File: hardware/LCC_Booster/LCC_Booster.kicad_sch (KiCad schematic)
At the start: 16 parts, among them J1 A00-216-262-450, J2 54-00166, J3 Screw_Terminal_01x08, SW1 SW_Push, U1 ACPL-214-500E, U2 ACPL-214-500E

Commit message: Update Schematic
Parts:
- removed C34, C35: C100n, Capacitor_SMD:C_0402_1005Metric_Pad0.74x0.62mm_HandSolder, symbol Device:C
- removed U1, U2: ACPL-214-500E, Package_SO:SOP-4_4.4x2.6mm_P1.27mm, symbol Isolator:ACPL-214-500E
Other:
- added sheet DCC Isolator (dcc_isolator.kicad_sch)
- moved on the sheet: A1, H1, H2, H3, H4, J1A, J1B, J2, J3, JP1, JP2, JP3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

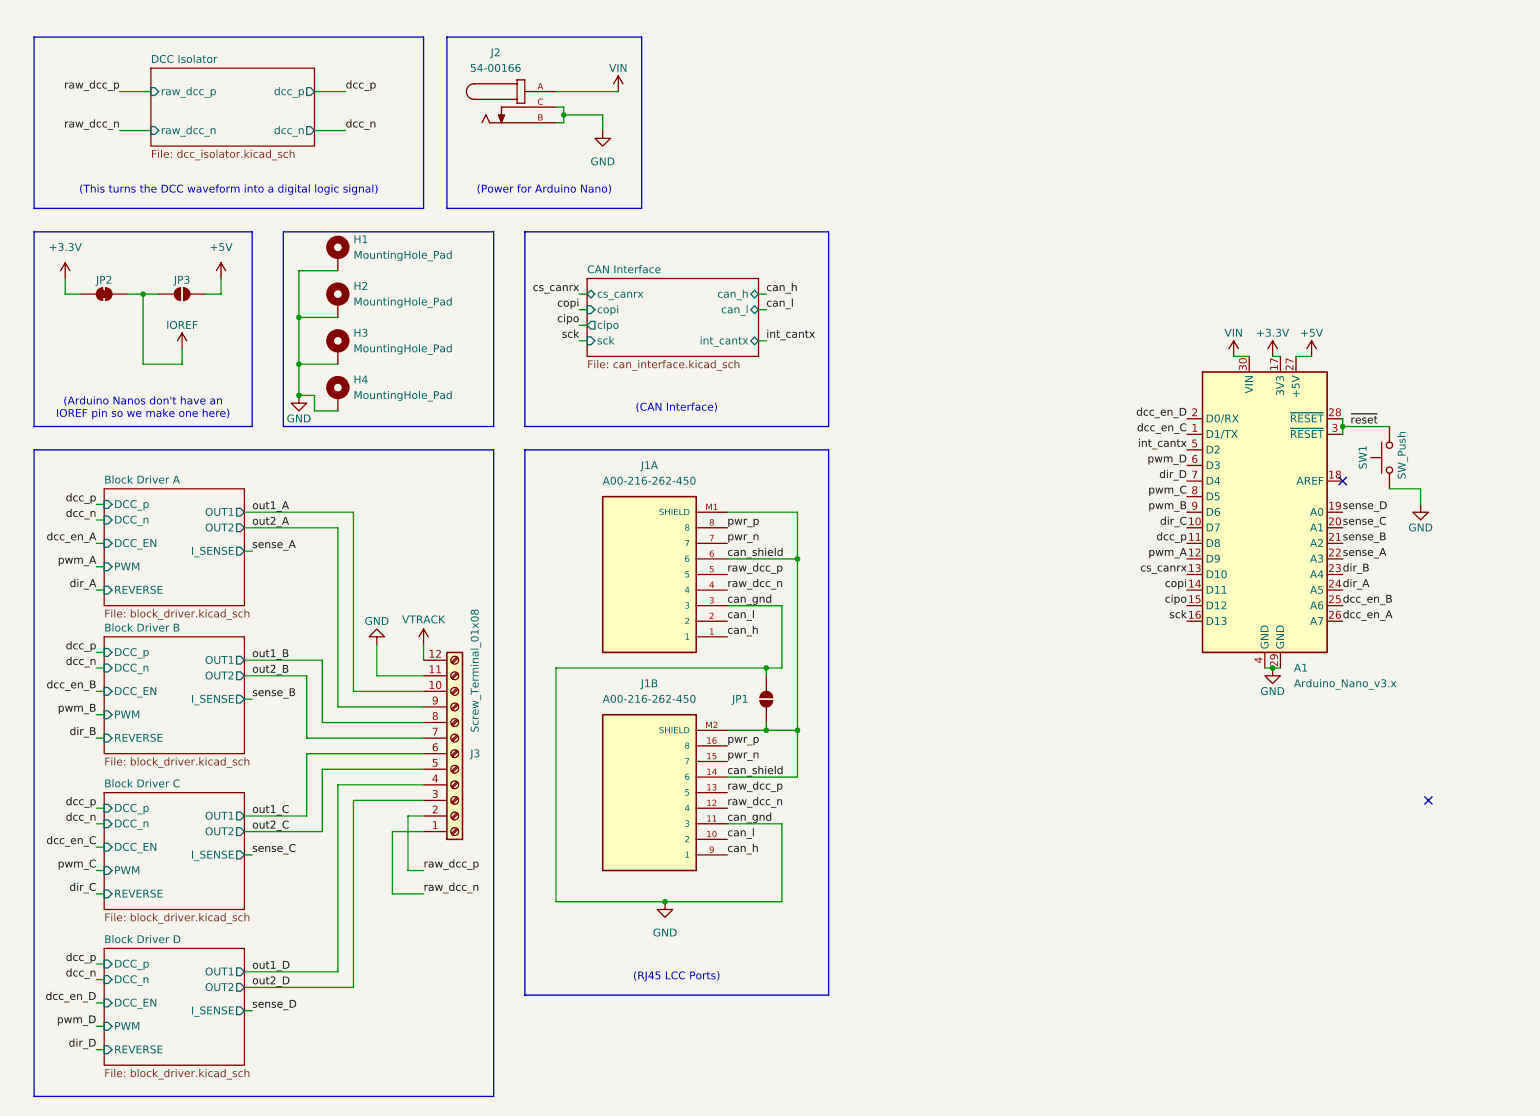
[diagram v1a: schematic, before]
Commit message: Add Fault Pin Inputs to Arduino
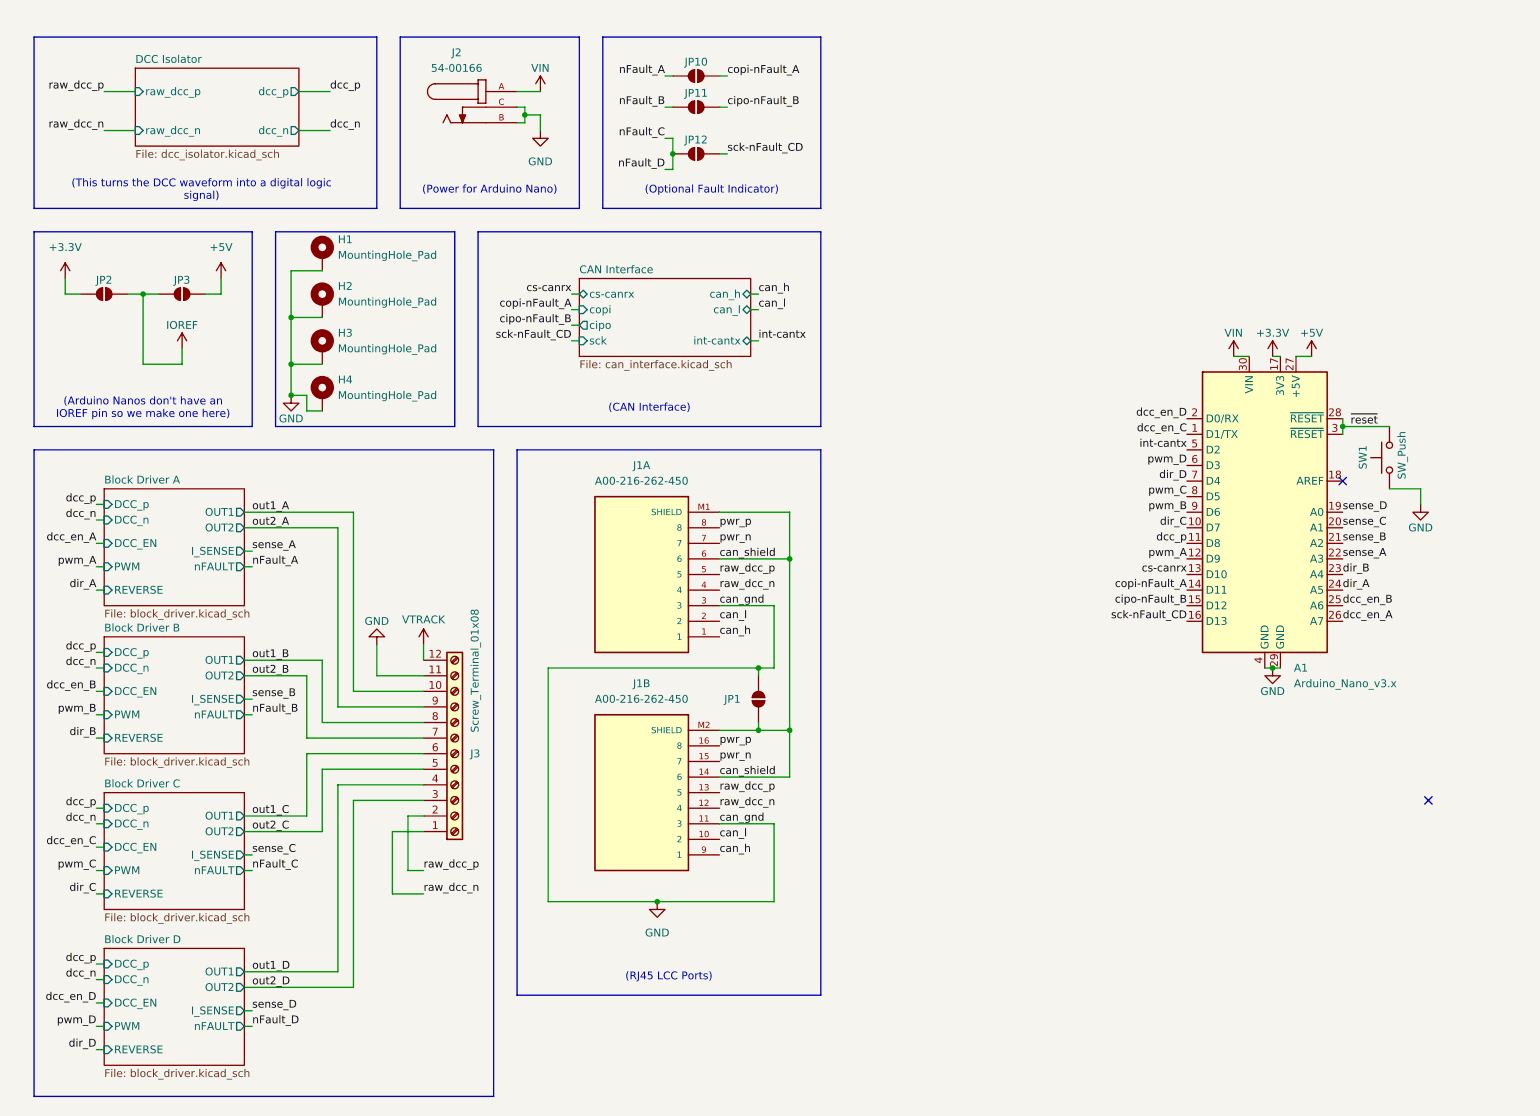
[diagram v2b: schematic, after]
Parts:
- removed JP2: SolderJumper_2_Open, Jumper:SolderJumper-2_P1.3mm_Bridged_RoundedPad1.0x1.5mm, symbol Jumper:SolderJumper_2_Bridged
- added JP10, JP11, JP12, JP2: SolderJumper_2_Open, Jumper:SolderJumper-2_P1.3mm_Open_RoundedPad1.0x1.5mm, symbol Jumper:SolderJumper_2_Open
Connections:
- net +3.3V: now also JP2.1 (A)
- net IOREF: now also JP2.2 (B)
- net cipo renamed cipo-nFault_B
- net cipo-nFault_B: now also JP11.2 (B)
- net copi renamed copi-nFault_A
- net copi-nFault_A: now also JP10.2 (B)
- net cs_canrx renamed cs-canrx
- net int_cantx renamed int-cantx
- net sck renamed sck-nFault_CD
- net sck-nFault_CD: now also JP12.2 (B)
- new net nFault_A: JP10.1 (A)
- new net nFault_B: JP11.1 (A)
- new net nFault_C: JP12.1 (A)
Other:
- sheet Block Driver A ports: added nFAULT; removed none
- sheet Block Driver B ports: added nFAULT; removed none
- sheet Block Driver C ports: added nFAULT; removed none
- sheet Block Driver D ports: added nFAULT; removed none
- sheet CAN Interface ports: added cs-canrx, int-cantx; removed cs_canrx, int_cantx
- moved on the sheet: H1, H2, H3, H4, J1A, J1B, J2, JP1

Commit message: Fix Some Hardware Pin Notations
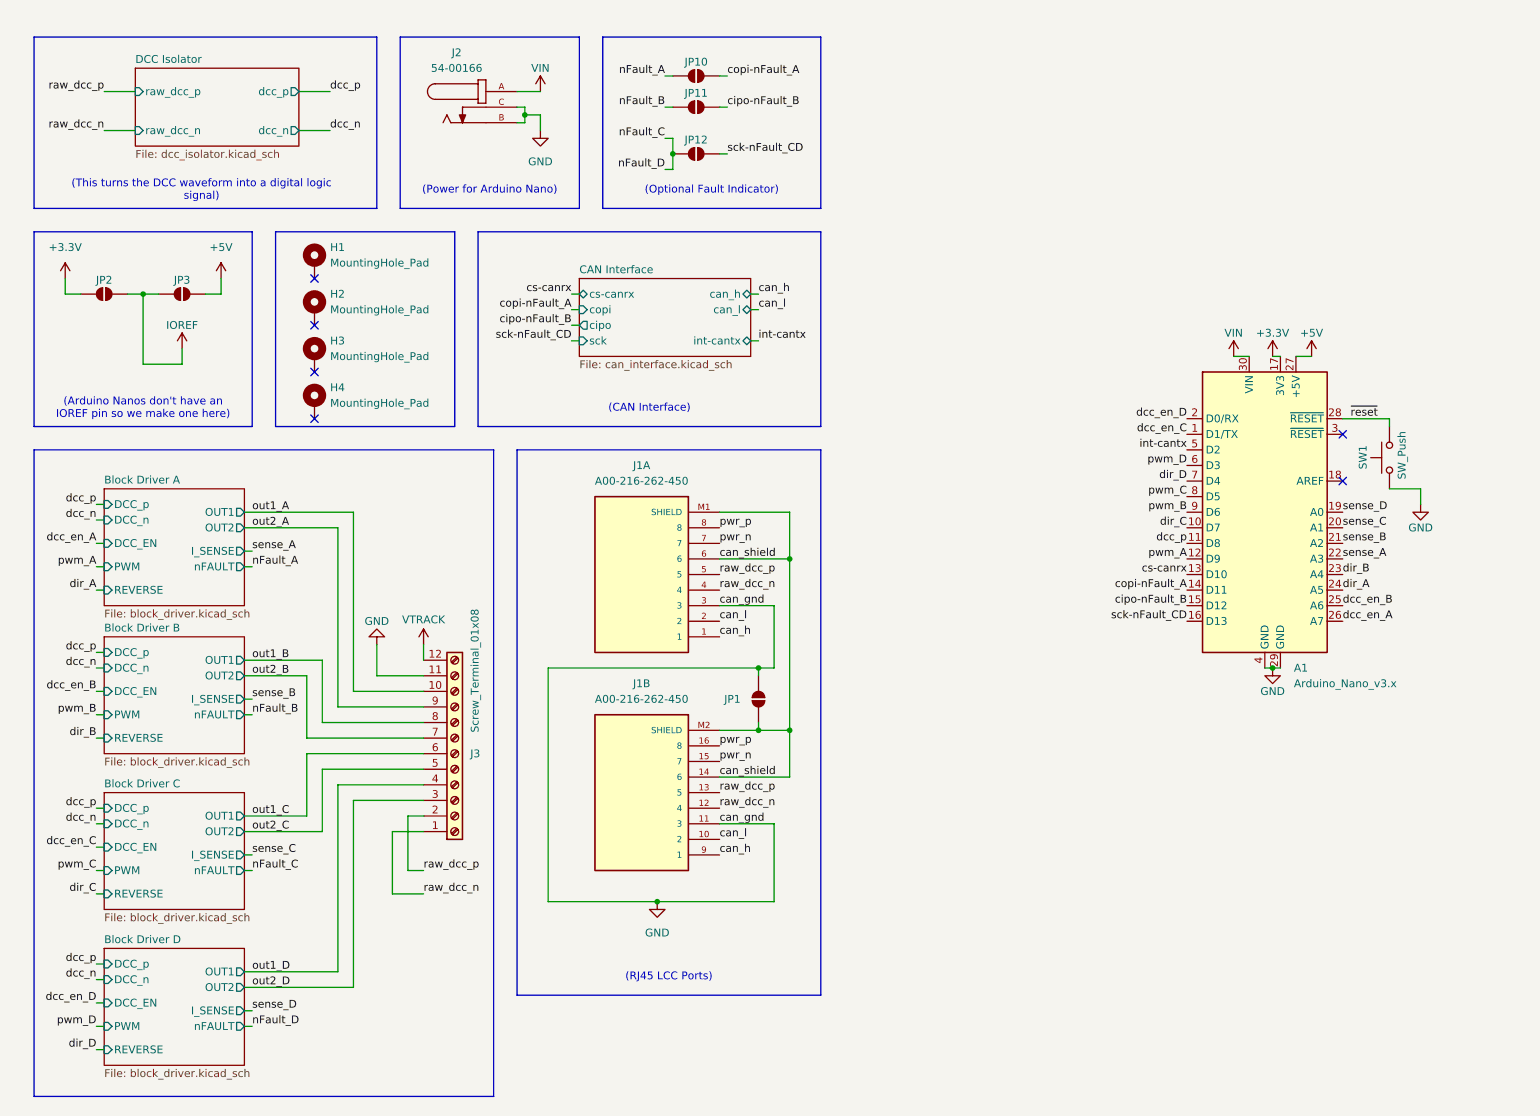
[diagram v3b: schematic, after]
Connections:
- net GND: no longer H1.1, H2.1, H3.1, H4.1
- net ~{reset}: no longer A1.3 (~{RESET})
- no-connect marks 2 -> 6
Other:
- moved on the sheet: H1, H2, H3, H4
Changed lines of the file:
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@@
 	)
 	(junction
-		(at 59.69 62.23)
-		(diameter 0)
-		(color 0 0 0 0)
-	)
-	(junction
-		(at 231.14 80.01)
-		(diameter 0)
-		(color 0 0 0 0)
-	)
-	(junction
-		(at 59.69 74.93)
-		(diameter 0)
-		(color 0 0 0 0)
-	)
-	(junction
 		(at 135.89 119.38)
 		(diameter 0)
@@
 	)
 	(junction
-		(at 59.69 69.85)
-		(diameter 0)
-		(color 0 0 0 0)
-	)
-	(junction
 		(at 219.71 119.38)
 		(diameter 0)
@@
 	)
 	(no_connect
+		(at 63.5 71.12)
+	)
+	(no_connect
 		(at 231.14 88.9)
 	)
 	(no_connect
-		(at 245.11 140.97)
+		(at 63.5 63.5)
+	)
+	(no_connect
+		(at 63.5 78.74)
+	)
+	(no_connect
+		(at 231.14 81.28)
+	)
+	(no_connect
+		(at 63.5 55.88)
 	)
 	(wire
@@
 	(wire
 		(pts
-			(xy 231.14 80.01) (xy 238.76 80.01)
+			(xy 231.14 78.74) (xy 238.76 78.74)
 		)
 		(stroke
@@
 	(wire
 		(pts
-			(xy 62.23 77.47) (xy 62.23 74.93)
-		)
-		(stroke
-			(width 0)
-			(type default)
-		)
-	)
-	(wire
-		(pts
 			(xy 52.07 168.91) (xy 67.31 168.91)
 		)
@@
 	(wire
 		(pts
-			(xy 27.94 106.68) (xy 29.21 106.68)
+			(xy 238.76 78.74) (xy 238.76 80.01)
 		)
 		(stroke
@@
 	(wire
 		(pts
-			(xy 59.69 62.23) (xy 59.69 69.85)
+			(xy 27.94 106.68) (xy 29.21 106.68)
 		)
 		(stroke
@@
 	(wire
 		(pts
-			(xy 231.14 78.74) (xy 231.14 80.01)
-		)
-		(stroke
-			(width 0)
-			(type default)
-		)
-	)
-	(wire
-		(pts
 			(xy 243.84 90.17) (xy 243.84 92.71)
 		)
@@
 	(wire
 		(pts
-			(xy 59.69 69.85) (xy 64.77 69.85)
-		)
-		(stroke
-			(width 0)
-			(type default)
-		)
-	)
-	(wire
-		(pts
 			(xy 120.65 33.02) (xy 121.92 33.02)
 		)
@@
 	(wire
 		(pts
-			(xy 62.23 74.93) (xy 59.69 74.93)
-		)
-		(stroke
-			(width 0)
-			(type default)
-		)
-	)
-	(wire
-		(pts
 			(xy 138.43 157.48) (xy 138.43 144.78)
 		)
@@
 	(wire
 		(pts
-			(xy 59.69 69.85) (xy 59.69 74.93)
-		)
-		(stroke
-			(width 0)
-			(type default)
-		)
-	)
-	(wire
-		(pts
 			(xy 243.84 90.17) (xy 238.76 90.17)
 		)
@@
 	(wire
 		(pts
-			(xy 59.69 62.23) (xy 64.77 62.23)
-		)
-		(stroke
-			(width 0)
-			(type default)
-		)
-	)
-	(wire
-		(pts
 			(xy 96.52 27.94) (xy 97.79 27.94)
 		)
@@
 	(wire
 		(pts
-			(xy 231.14 80.01) (xy 231.14 81.28)
-		)
-		(stroke
-			(width 0)
-			(type default)
-		)
-	)
-	(wire
-		(pts
 			(xy 27.94 142.24) (xy 29.21 142.24)
 		)
@@
 	(wire
 		(pts
-			(xy 59.69 54.61) (xy 59.69 62.23)
-		)
-		(stroke
-			(width 0)
-			(type default)
-		)
-	)
-	(wire
-		(pts
 			(xy 105.41 60.96) (xy 106.68 60.96)
 		)
@@
 	(wire
 		(pts
-			(xy 64.77 77.47) (xy 62.23 77.47)
-		)
-		(stroke
-			(width 0)
-			(type default)
-		)
-	)
-	(wire
-		(pts
 			(xy 27.94 148.59) (xy 29.21 148.59)
 		)
@@
 	(wire
 		(pts
-			(xy 64.77 54.61) (xy 59.69 54.61)
-		)
-		(stroke
-			(width 0)
-			(type default)
-		)
-	)
-	(wire
-		(pts
 			(xy 120.65 38.1) (xy 121.92 38.1)
 		)
@@
 	)
 	(label "~{reset}"
-		(at 232.41 80.01 0)
+		(at 232.41 78.74 0)
 		(fields_autoplaced yes)
 		(effects
@@
 	(symbol
 		(lib_id "Mechanical:MountingHole_Pad")
-		(at 64.77 59.69 0)
+		(at 63.5 60.96 0)
 		(unit 1)
 		(exclude_from_sim yes)
@@
 		(dnp no)
 		(property "Reference" "H2"
-			(at 67.31 57.1499 0)
+			(at 66.04 58.4199 0)
 			(effects
 				(font
@@
 		)
 		(property "Value" "MountingHole_Pad"
-			(at 67.31 59.6899 0)
+			(at 66.04 60.9599 0)
 			(effects
 				(font
@@
 		)
 		(property "Footprint" "MountingHole:MountingHole_4.3mm_M4_Pad_Via"
-			(at 64.77 59.69 0)
+			(at 63.5 60.96 0)
 			(effects
 				(font
@@
 		)
 		(property "Datasheet" "~"
-			(at 64.77 59.69 0)
+			(at 63.5 60.96 0)
 			(effects
 				(font
@@
 		)
 		(property "Description" "Mounting Hole with connection"
-			(at 64.77 59.69 0)
+			(at 63.5 60.96 0)
 			(effects
 				(font
@@
 	(symbol
 		(lib_id "Mechanical:MountingHole_Pad")
-		(at 64.77 52.07 0)
+		(at 63.5 53.34 0)
 		(unit 1)
 		(exclude_from_sim yes)
@@
 		(fields_autoplaced yes)
 		(property "Reference" "H1"
-			(at 67.31 49.5299 0)
+			(at 66.04 50.7999 0)
 			(effects
 				(font
@@
 		)
 		(property "Value" "MountingHole_Pad"
-			(at 67.31 52.0699 0)
+			(at 66.04 53.3399 0)
 			(effects
 				(font
@@
 		)
 		(property "Footprint" "MountingHole:MountingHole_4.3mm_M4_Pad_Via"
-			(at 64.77 52.07 0)
+			(at 63.5 53.34 0)
 			(effects
 				(font
@@
 		)
 		(property "Datasheet" "~"
-			(at 64.77 52.07 0)
+			(at 63.5 53.34 0)
 			(effects
 				(font
@@
 		)
 		(property "Description" "Mounting Hole with connection"
-			(at 64.77 52.07 0)
+			(at 63.5 53.34 0)
 			(effects
 				(font
@@
 	)
 	(symbol
-		(lib_id "power:GND")
-		(at 59.69 74.93 0)
-		(unit 1)
-		(exclude_from_sim no)
-		(in_bom yes)
-		(on_board yes)
-		(dnp no)
-		(property "Reference" "#PWR012"
-			(at 59.69 81.28 0)
-			(effects
-				(font
-					(size 1.27 1.27)
-				)
-				(hide yes)
-			)
-		)
-		(property "Value" "GND"
-			(at 59.69 78.74 0)
-			(effects
-				(font
-					(size 1.27 1.27)
-				)
-			)
-		)
-		(property "Footprint" ""
-			(at 59.69 74.93 0)
-			(effects
-				(font
-					(size 1.27 1.27)
-				)
-				(hide yes)
-			)
-		)
-		(property "Datasheet" ""
-			(at 59.69 74.93 0)
-			(effects
-				(font
-					(size 1.27 1.27)
-				)
-				(hide yes)
-			)
-		)
-		(property "Description" "Power symbol creates a global label with name \"GND\" , ground"
-			(at 59.69 74.93 0)
-			(effects
-				(font
-					(size 1.27 1.27)
-				)
-				(hide yes)
-			)
-		)
-		(pin "1"
-		)
-		(instances
-			(project "LCC_Booster"
-				(path "/e8524381-bb01-4107-93ec-8133e878a3da"
-					(reference "#PWR012")
-					(unit 1)
-				)
-			)
-		)
-	)
-	(symbol
 		(lib_id "Mechanical:MountingHole_Pad")
-		(at 64.77 74.93 0)
+		(at 63.5 76.2 0)
 		(unit 1)
 		(exclude_from_sim yes)
@@
 		(fields_autoplaced yes)
 		(property "Reference" "H4"
-			(at 67.31 72.3899 0)
+			(at 66.04 73.6599 0)
 			(effects
 				(font
@@
 		)
 		(property "Value" "MountingHole_Pad"
-			(at 67.31 74.9299 0)
+			(at 66.04 76.1999 0)
 			(effects
 				(font
@@
 		)
 		(property "Footprint" "MountingHole:MountingHole_4.3mm_M4_Pad_Via"
-			(at 64.77 74.93 0)
+			(at 63.5 76.2 0)
 			(effects
 				(font
@@
 		)
 		(property "Datasheet" "~"
-			(at 64.77 74.93 0)
+			(at 63.5 76.2 0)
 			(effects
 				(font
@@
 		)
 		(property "Description" "Mounting Hole with connection"
-			(at 64.77 74.93 0)
+			(at 63.5 76.2 0)
 			(effects
 				(font
@@
 	(symbol
 		(lib_id "Mechanical:MountingHole_Pad")
-		(at 64.77 67.31 0)
+		(at 63.5 68.58 0)
 		(unit 1)
 		(exclude_from_sim yes)
@@
 		(fields_autoplaced yes)
 		(property "Reference" "H3"
-			(at 67.31 64.7699 0)
+			(at 66.04 66.0399 0)
 			(effects
 				(font
@@
 		)
 		(property "Value" "MountingHole_Pad"
-			(at 67.31 67.3099 0)
+			(at 66.04 68.5799 0)
 			(effects
 				(font
@@
 		)
 		(property "Footprint" "MountingHole:MountingHole_4.3mm_M4_Pad_Via"
-			(at 64.77 67.31 0)
+			(at 63.5 68.58 0)
 			(effects
 				(font
@@
 		)
 		(property "Datasheet" "~"
-			(at 64.77 67.31 0)
+			(at 63.5 68.58 0)
 			(effects
 				(font
@@
 		)
 		(property "Description" "Mounting Hole with connection"
-			(at 64.77 67.31 0)
+			(at 63.5 68.58 0)
 			(effects
 				(font

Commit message: Update for PCB Assembly
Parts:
- removed J1: A00-216-262-450, A00_216_262_450:EDAC_A00-216-262-450, symbol A00-216-262-450:A00-216-262-450
- removed JP1: SolderJumper_2_Open, Jumper:SolderJumper-2_P1.3mm_Open_RoundedPad1.0x1.5mm, symbol Jumper:SolderJumper_2_Open
- added J3: RJHSE508002, RJHSE508002:AMPHENOL_RJHSE508002, symbol RJHSE508002:RJHSE508002
- A1: MANUFACTURER (none) -> STMicroelectronics; Manufacturer Part Number (none) -> L432KC
- J1: renamed from J3; MANUFACTURER (none) -> Phoenix Contact; Manufacturer Part Number (none) -> 1753611
- J2, SW1: now not fitted
- renumbered JP2 to JP1, JP3 to JP2, JP10 to JP3, JP11 to JP4, JP12 to JP5
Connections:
- net GND: now also J3.1_3, J3.2_3
- net can_h: now also J3.1_1, J3.2_1
- net can_l: now also J3.1_2, J3.2_2
- net can_shield: now also J3.1_6, J3.2_6
- net pwr_n: now also J3.1_7, J3.2_7
- net pwr_p: now also J3.1_8, J3.2_8
- net raw_dcc_n: now also J3.1_4, J3.2_4
- net raw_dcc_p: now also J3.1_5, J3.2_5
